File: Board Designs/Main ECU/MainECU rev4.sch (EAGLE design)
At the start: 164 parts, among them Q10 MMBT3904LT3G, Q11 MMBT3904LT3G, Q9 MMBT3904LT3G, X1 CONNECTOR-37, X2 CONNECTOR-4AUTOSPORT, X3 CONNECTOR-4NANO-FIT-VERTICAL-4, X4 CONNECTOR-4NANO-FIT-VERTICAL-4

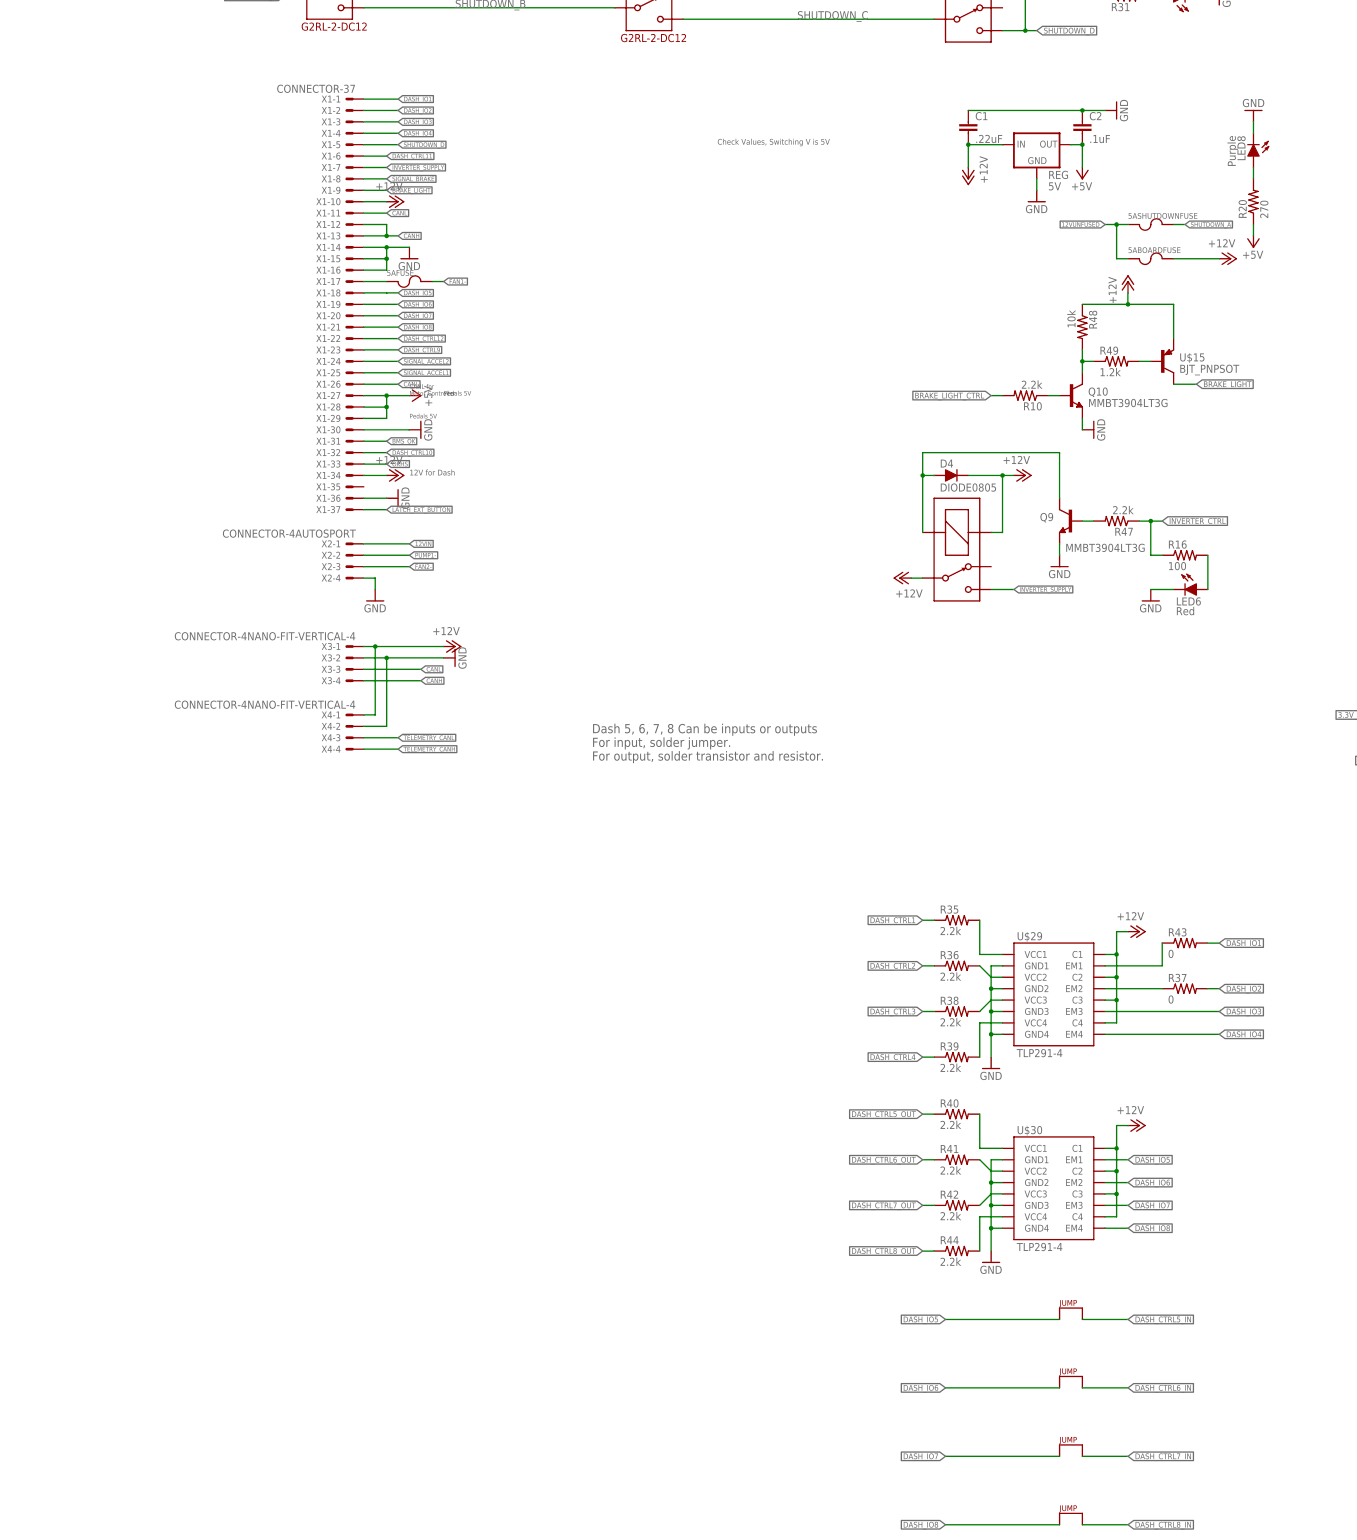
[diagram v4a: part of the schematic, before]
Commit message: Main ECU rev4: Flip transistors to top layer, widen inverter supply trace, move some resistors for easier soldering, adjust dashboard control resistor values, clean up schematic
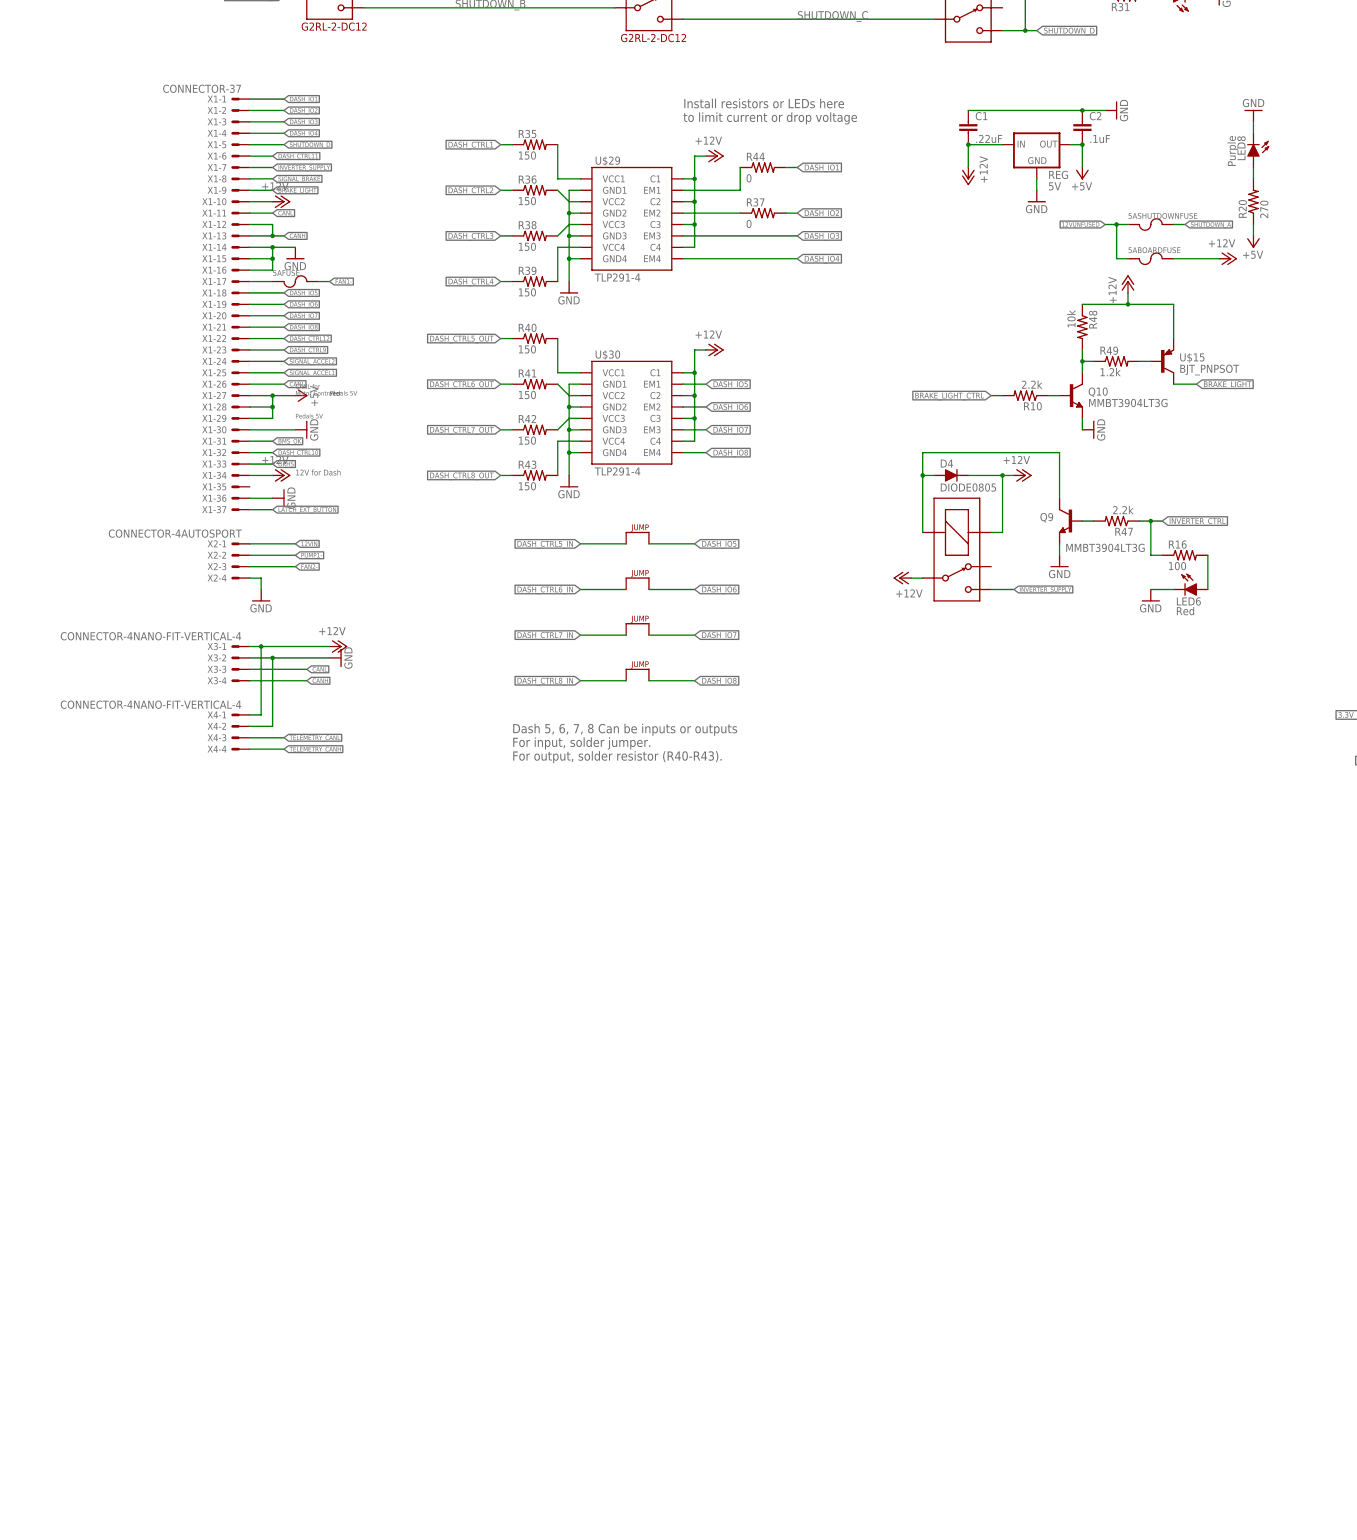
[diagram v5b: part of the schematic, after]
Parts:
- R35, R36, R38, R39, R40, R41, R42: value 2.2k -> 150
- R43: value 0 -> 150
- R44: value 2.2k -> 0
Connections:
- net DASH_CTRL8_OUT: now also R43.1; no longer R44.1
- net DASH_IO1: now also R44.2; no longer R43.2
- net N$57: now also R43.2; no longer R44.2
- net N$59: now also R44.1; no longer R43.1
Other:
- note added: "Dash 5, 6, 7, 8 Can be inputs or outputs For input, solder jumper. For output, solder resistor (R40-R43)."
- note added: "Install resistors or LEDs here to limit current or drop voltage"
- note removed: "Check Values, Switching V is 5V"
- note removed: "Dash 5, 6, 7, 8 Can be inputs or outputs For input, solder jumper. For output, solder transistor and resistor."
- moved on the sheet: 5AFUSE, R35, R36, R37, R38, R39, R40, R41, R42, R43, R44, U$29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

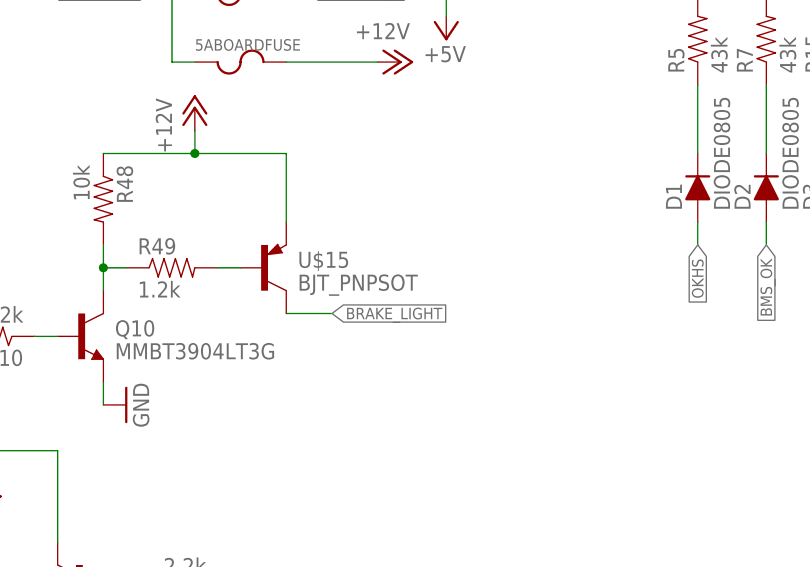
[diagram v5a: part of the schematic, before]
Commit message: Main ECU rev{2,4}: Specify PNP transistor P/Ns
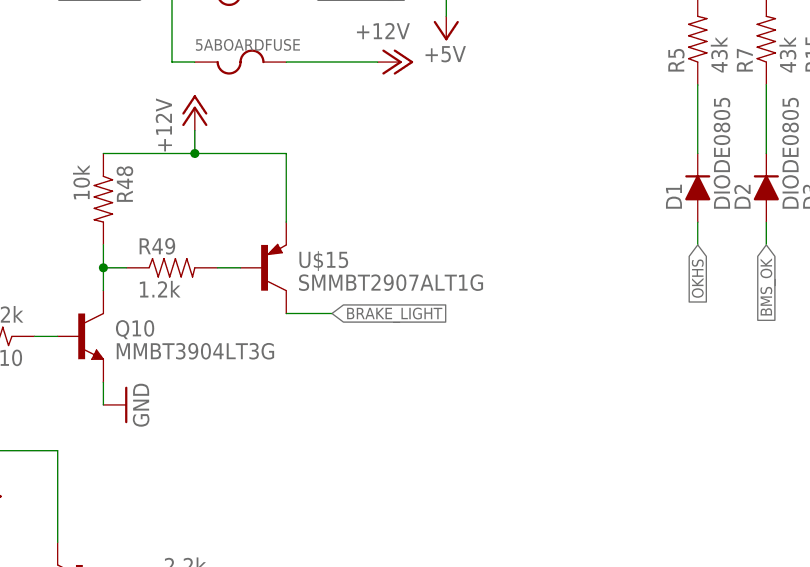
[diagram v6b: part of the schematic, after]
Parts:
- U$15: value BJT_PNPSOT -> SMMBT2907ALT1G
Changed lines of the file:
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@@
 <part name="P+9" library="supply1" deviceset="+12V" device=""/>
 <part name="Q10" library="HyTechDevices" deviceset="BJT_NPN" device="SOT" value="MMBT3904LT3G"/>
-<part name="U$15" library="HyTechDevices" deviceset="BJT_PNP" device="SOT"/>
+<part name="U$15" library="HyTechDevices" deviceset="BJT_PNP" device="SOT" value="SMMBT2907ALT1G"/>
 <part name="R10" library="HyTechDevices" deviceset="RESISTOR" device="0805-RES" value="2.2k"/>
 <part name="R48" library="HyTechDevices" deviceset="RESISTOR" device="0805-RES" value="10k"/>

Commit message: Main ECU rev{1-4}: Add warning about RTC cell assembly, specify current sensor input capacitor value, lower XBee LED resistor to 33R; Main ECU rev{2,4}: Specify MCP3208 input capacitor value; Main ECU rev4: Lower relay-controlling transistors' base resistor to 1k; Main ECU rev5: make all relevant changes previously listed
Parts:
- C10, C9: value (none) -> 0.1uF
- C11: value (none) -> 1uF
- R45: value 2.3k -> 33
- R47, R50: value 2.2k -> 1k
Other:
- note added: "Do not connect RTC batt to 3.3V_2➡ Must cut line and connect to VBAT➡"
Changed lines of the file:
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@@
 <part name="C7" library="HyTechDevices" deviceset="CAP" device="0805"/>
 <part name="C8" library="HyTechDevices" deviceset="CAP" device="0805"/>
-<part name="C9" library="HyTechDevices" deviceset="CAP" device="0805"/>
-<part name="C10" library="HyTechDevices" deviceset="CAP" device="0805"/>
+<part name="C9" library="HyTechDevices" deviceset="CAP" device="0805" value="0.1uF"/>
+<part name="C10" library="HyTechDevices" deviceset="CAP" device="0805" value="0.1uF"/>
 <part name="GND46" library="HyTechSymbols" deviceset="GND" device=""/>
 <part name="GND47" library="HyTechSymbols" deviceset="GND" device=""/>
@@
 <part name="P+35" library="supply1" library_urn="urn:adsk.eagle:library:371" deviceset="+5V" device=""/>
 <part name="LED14" library="HyTechDevices" deviceset="LED" device="-0805" value="Blue"/>
-<part name="R45" library="HyTechDevices" deviceset="RESISTOR" device="0805-RES" value="2.3k"/>
+<part name="R45" library="HyTechDevices" deviceset="RESISTOR" device="0805-RES" value="33"/>
 <part name="GND62" library="HyTechSymbols" deviceset="GND" device=""/>
 <part name="X3" library="HyTechDevices" deviceset="CONNECTOR-4" device="NANO-FIT-VERTICAL-4"/>
@@
 <part name="GND40" library="HyTechSymbols" deviceset="GND" device=""/>
 <part name="P+32" library="supply1" deviceset="+12V" device=""/>
-<part name="C11" library="HyTechDevices" deviceset="CAP" device="0805"/>
+<part name="C11" library="HyTechDevices" deviceset="CAP" device="0805" value="1uF"/>
 <part name="CAN_TRANSCEIVER2" library="HyTechDevices" deviceset="MCP2551" device="" value="MCP2551"/>
 <part name="GND51" library="HyTechSymbols" deviceset="GND" device=""/>
@@
 <part name="R46" library="HyTechDevices" deviceset="RESISTOR" device="0805-RES" value="120"/>
 <part name="Q9" library="HyTechDevices" deviceset="BJT_NPN" device="SOT" value="MMBT3904LT3G"/>
-<part name="R47" library="HyTechDevices" deviceset="RESISTOR" device="0805-RES" value="2.2k"/>
+<part name="R47" library="HyTechDevices" deviceset="RESISTOR" device="0805-RES" value="1k"/>
 <part name="GND56" library="HyTechSymbols" deviceset="GND" device=""/>
 <part name="Q11" library="HyTechDevices" deviceset="BJT_NPN" device="SOT" value="MMBT3904LT3G"/>
 <part name="GND11" library="HyTechSymbols" deviceset="GND" device=""/>
-<part name="R50" library="HyTechDevices" deviceset="RESISTOR" device="0805-RES" value="2.2k"/>
+<part name="R50" library="HyTechDevices" deviceset="RESISTOR" device="0805-RES" value="1k"/>
 <part name="FLIP" library="supply1" library_urn="urn:adsk.eagle:library:371" deviceset="+5V" device=""/>
 <part name="GND42" library="HyTechSymbols" deviceset="GND" device=""/>
@@
 <wire x1="165.1" y1="165.1" x2="165.1" y2="0" width="0.1524" layer="90"/>
 <text x="165.1" y="165.1" size="3.81" layer="90">Power</text>
-<text x="419.1" y="264.16" size="1.778" layer="97">ECU Current Sensor</text>
-<text x="419.1" y="231.14" size="1.778" layer="97">Cooling Current Sensor</text>
+<text x="416.56" y="264.16" size="1.778" layer="97">ECU Current Sensor</text>
+<text x="416.56" y="231.14" size="1.778" layer="97">Cooling Current Sensor</text>
 <text x="264.16" y="236.22" size="1.778" layer="91">Pullup/down resistors to
 detect open circuit. Install
@@
 <text x="119.38" y="154.94" size="2.032" layer="96">Install resistors or LEDs here
 to limit current or drop voltage</text>
+<text x="439.42" y="58.42" size="1.778" layer="91" align="top-right">Do not connect RTC batt to 3.3V_2➡
+Must cut line and connect to VBAT➡</text>
 </plain>
 <instances>
@@
 <attribute name="VALUE" x="455.676" y="233.299" size="1.778" layer="96" rot="R180"/>
 </instance>
-<instance part="GND46" gate="1" x="452.12" y="233.68" smashed="yes" rot="R270">
-<attribute name="VALUE" x="449.58" y="236.22" size="1.778" layer="96" rot="R270"/>
+<instance part="GND46" gate="1" x="447.04" y="233.68" smashed="yes" rot="R270">
+<attribute name="VALUE" x="444.5" y="236.22" size="1.778" layer="96" rot="R270"/>
 </instance>
-<instance part="GND47" gate="1" x="452.12" y="266.7" smashed="yes" rot="R270">
-<attribute name="VALUE" x="449.58" y="269.24" size="1.778" layer="96" rot="R270"/>
+<instance part="GND47" gate="1" x="447.04" y="266.7" smashed="yes" rot="R270">
+<attribute name="VALUE" x="444.5" y="269.24" size="1.778" layer="96" rot="R270"/>
 </instance>
 <instance part="GND15" gate="1" x="408.94" y="213.36" smashed="yes">
@@
 <pinref part="GND46" gate="1" pin="GND"/>
 <pinref part="C10" gate="G$1" pin="2"/>
-<wire x1="454.66" y1="233.68" x2="457.2" y2="233.68" width="0.1524" layer="91"/>
+<wire x1="449.58" y1="233.68" x2="457.2" y2="233.68" width="0.1524" layer="91"/>
 </segment>
 <segment>
@@
 <pinref part="GND47" gate="1" pin="GND"/>
 <pinref part="C9" gate="G$1" pin="2"/>
-<wire x1="454.66" y1="266.7" x2="457.2" y2="266.7" width="0.1524" layer="91"/>
+<wire x1="449.58" y1="266.7" x2="457.2" y2="266.7" width="0.1524" layer="91"/>
 </segment>
 <segment>
@@
 <pinref part="IMD_SHUTDOWN1" gate="G$1" pin="4"/>
 <wire x1="104.14" y1="210.82" x2="104.14" y2="220.98" width="0.1524" layer="91"/>
-<wire x1="119.38" y1="187.96" x2="147.32" y2="187.96" width="0.1524" layer="91"/>
-<wire x1="147.32" y1="187.96" x2="139.7" y2="187.96" width="0.1524" layer="91"/>
+<wire x1="119.38" y1="187.96" x2="139.7" y2="187.96" width="0.1524" layer="91"/>
+<wire x1="139.7" y1="187.96" x2="147.32" y2="187.96" width="0.1524" layer="91"/>
 <wire x1="139.7" y1="187.96" x2="139.7" y2="200.66" width="0.1524" layer="91"/>
 <junction x="104.14" y="210.82"/>
 <pinref part="R17" gate="G$1" pin="1"/>
-<junction x="147.32" y="187.96"/>
 <label x="111.76" y="210.82" size="1.778" layer="95"/>
 <wire x1="139.7" y1="200.66" x2="139.7" y2="210.82" width="0.1524" layer="91"/>
@@
 <wire x1="132.08" y1="200.66" x2="139.7" y2="200.66" width="0.1524" layer="91"/>
 <junction x="139.7" y="200.66"/>
+<junction x="139.7" y="187.96"/>
 </segment>
 </net>
@@
 <wire x1="424.18" y1="38.1" x2="419.1" y2="38.1" width="0.1524" layer="91"/>
 <junction x="424.18" y="38.1"/>
-<label x="419.1" y="55.88" size="1.27" layer="95" xref="yes"/>
-<wire x1="419.1" y1="38.1" x2="419.1" y2="55.88" width="0.1524" layer="91"/>
+<label x="419.1" y="48.26" size="1.27" layer="95" xref="yes"/>
+<wire x1="419.1" y1="38.1" x2="419.1" y2="48.26" width="0.1524" layer="91"/>
 <pinref part="C21" gate="G$1" pin="2"/>
 <junction x="401.32" y="38.1"/>
 <pinref part="REG3" gate="G$1" pin="OUT"/>
 <wire x1="401.32" y1="35.56" x2="401.32" y2="38.1" width="0.1524" layer="91"/>
-<wire x1="406.4" y1="38.1" x2="401.32" y2="38.1" width="0.1524" layer="91"/>
-<wire x1="406.4" y1="38.1" x2="419.1" y2="38.1" width="0.1524" layer="91"/>
+<wire x1="401.32" y1="38.1" x2="419.1" y2="38.1" width="0.1524" layer="91"/>
 <junction x="419.1" y="38.1"/>
 </segment>
